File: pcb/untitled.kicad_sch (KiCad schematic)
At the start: 6 parts, among them Q1 NMOS, Q2 PMOS

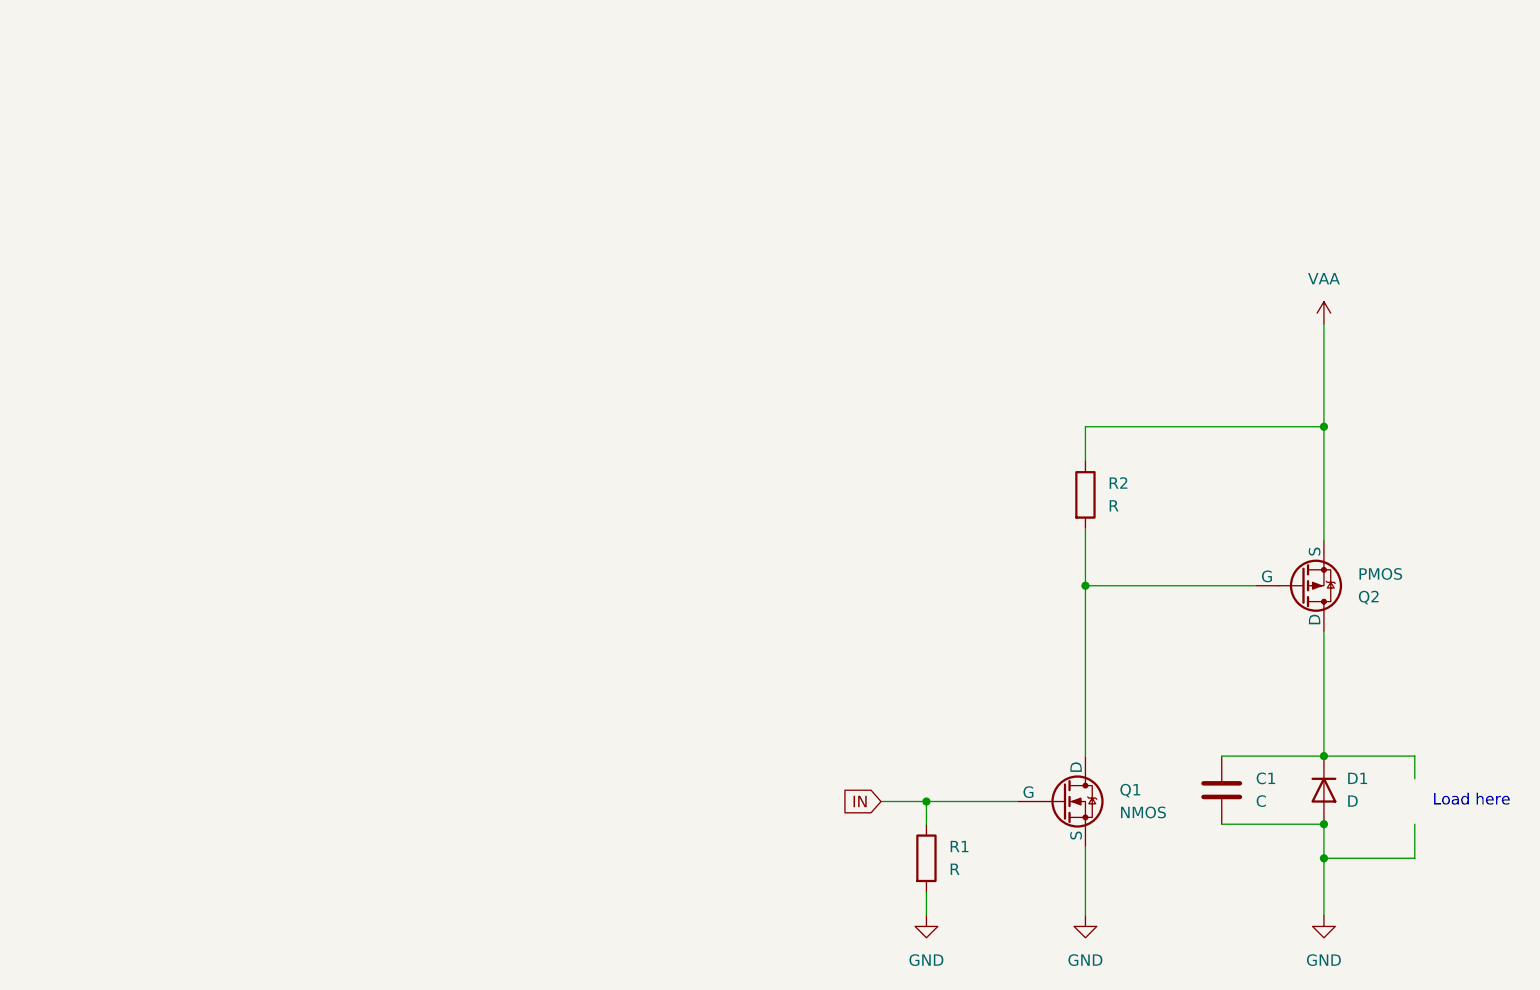
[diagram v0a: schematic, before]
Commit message: Upload of rcs controller board 1st draft
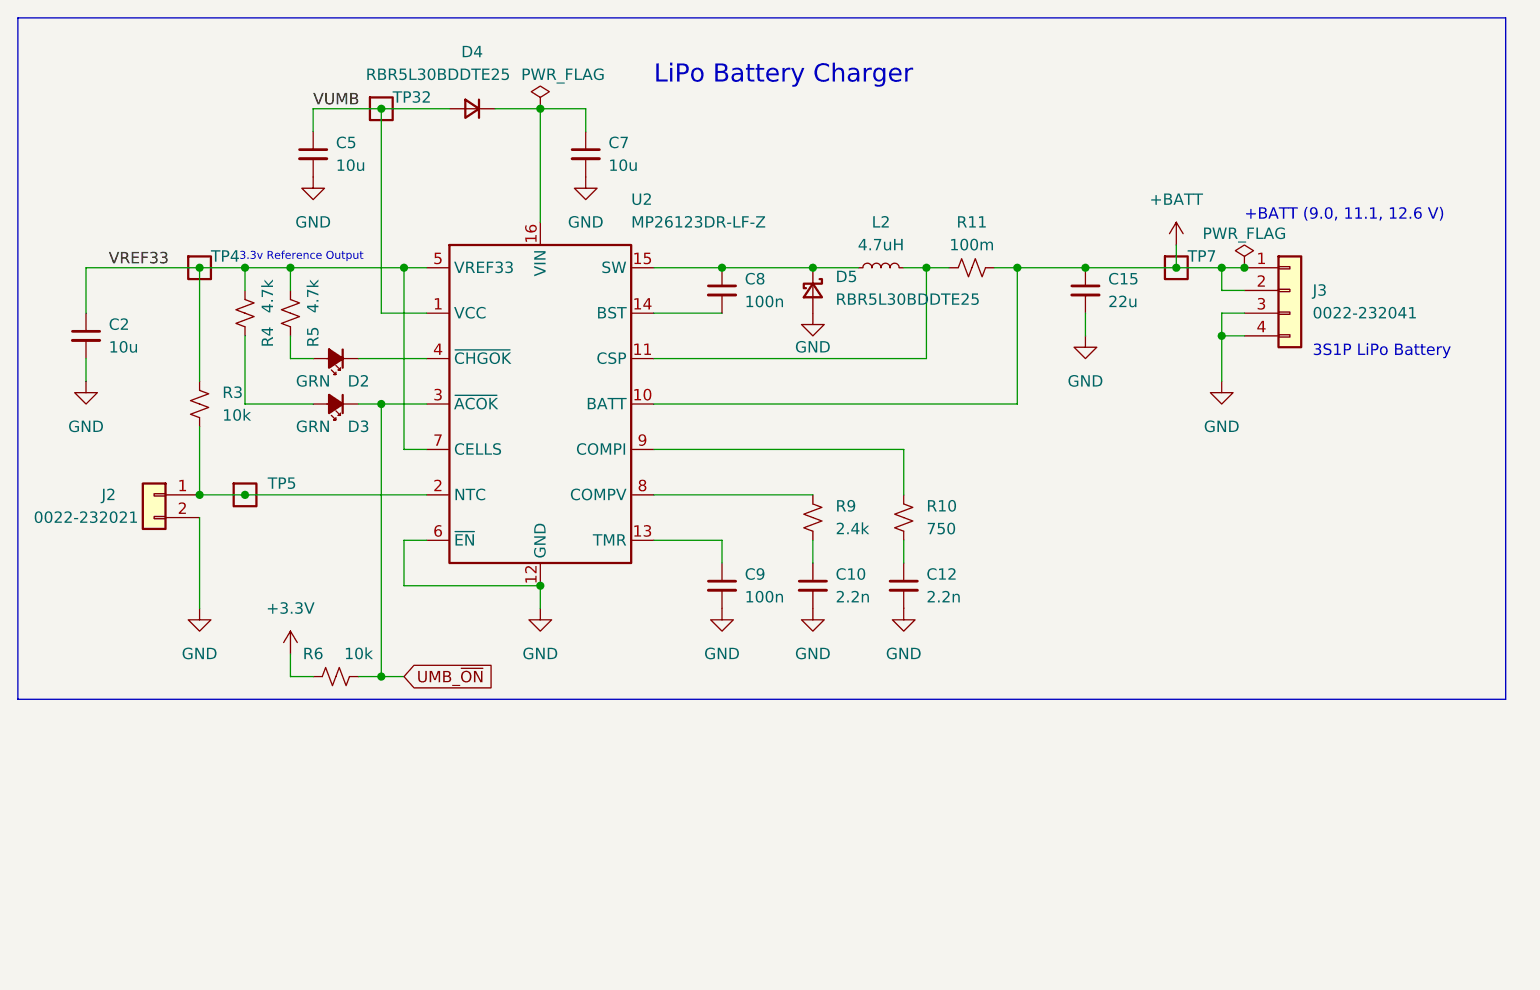
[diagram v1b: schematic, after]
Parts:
- removed C1: C, symbol Device:C
- removed D1: D, symbol Device:D
- removed Q1: NMOS, symbol Simulation_SPICE:NMOS
- removed Q2: PMOS, symbol Simulation_SPICE:PMOS
- removed R1, R2: R, symbol Device:R
- added C10, C12: 2.2n, Capacitor_SMD:C_0603_1608Metric, symbol Device:C_Small
- added C15: 22u, Capacitor_SMD:C_0805_2012Metric, symbol Device:C_Small
- added C2, C5, C7: 10u, Capacitor_SMD:C_0805_2012Metric, symbol Device:C_Small
- added C8, C9: 100n, Capacitor_SMD:C_0603_1608Metric, symbol Device:C_Small
- added D2, D3: GRN, LED_SMD:LED_0603_1608Metric, symbol Device:LED_Small_Filled
- added D4: RBR5L30BDDTE25, Diode_SMD:D_SMA, symbol Device:D_Small
- added D5: RBR5L30BDDTE25, Diode_SMD:D_SMA, symbol Device:D_Schottky_Small
- added J2: 0022-232021, Connector_Molex:Molex_KK-254_AE-6410-02A_1x02_P2.54mm_Vertical, symbol Connector_Generic:Conn_01x02
- added J3: 0022-232041, Connector_Molex:Molex_KK-254_AE-6410-04A_1x04_P2.54mm_Vertical, symbol Connector_Generic:Conn_01x04
- added L2: 4.7uH, Inductor_SMD:L_Vishay_IHLP-2020, symbol Device:L_Small
- added R10: 750, Resistor_SMD:R_0603_1608Metric, symbol Device:R_Small_US
- added R11: 100m, Resistor_SMD:R_1206_3216Metric, symbol Device:R_Small_US
- added R3, R6: 10k, Resistor_SMD:R_0603_1608Metric, symbol Device:R_Small_US
- added R4, R5: 4.7k, Resistor_SMD:R_0603_1608Metric, symbol Device:R_Small_US
- added R9: 2.4k, Resistor_SMD:R_0603_1608Metric, symbol Device:R_Small_US
- added TP32, TP4, TP5, TP7: Test-Point, psas-footprints:TP-through-hole-1X01, symbol psas-testpoint:Test-Point
- added U2: MP26123DR-LF-Z, Package_DFN_QFN:QFN-16-1EP_4x4mm_P0.65mm_EP2.5x2.5mm, symbol U-MonolithicPower-MP26123DR-LF-Z-battery-charger-li-ion:MP26123DR-LF-Z
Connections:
- net GND: now also C10.2, C12.2, C15.2, C2.2, C5.2, C7.2, C9.2, D5.2 (A), J2.2 (Pin_2), J3.3 (Pin_3), J3.4 (Pin_4), U2.12 (GND), U2.17 (GND), U2.6 (~{EN})
- new net: C12.1, R10.2
- new net: D3.2 (A), R4.2
- new net: C8.1, D5.1 (K), L2.1, U2.15 (SW)
- new net: L2.2, R11.1, U2.11 (CSP)
- new net: R9.1, U2.8 (COMPV)
- new net: C10.1, R9.2
- new net: D2.1 (K), U2.4 (~{CHGOK})
- new net: D2.2 (A), R5.2
- new net: J2.1 (Pin_1), R3.2, TP5.1, U2.2 (NTC)
- new net: C7.1, D4.1 (K), U2.16 (VIN)
- new net: C8.2, U2.14 (BST)
- new net: C9.1, U2.13 (TMR)
- new net: R10.1, U2.9 (COMPI)
- new net +3.3V: R6.1
- new net +BATT: C15.1, J3.1 (Pin_1), J3.2 (Pin_2), R11.2, TP7.1, U2.10 (BATT)
- new net UMB_~{ON}: D3.1 (K), R6.2, U2.3 (~{ACOK})
- new net VREF33: C2.1, R3.1, R4.1, R5.1, TP4.1, U2.5 (VREF33), U2.7 (CELLS)
- new net VUMB: C5.1, D4.2 (A), TP32.1, U2.1 (VCC)
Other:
- note added: "+BATT (9.0, 11.1, 12.6 V)"
- note added: "3.3v Reference Output"
- note added: "3S1P LiPo Battery"
- note added: "LiPo Battery Charger"
- note removed: "Load here"

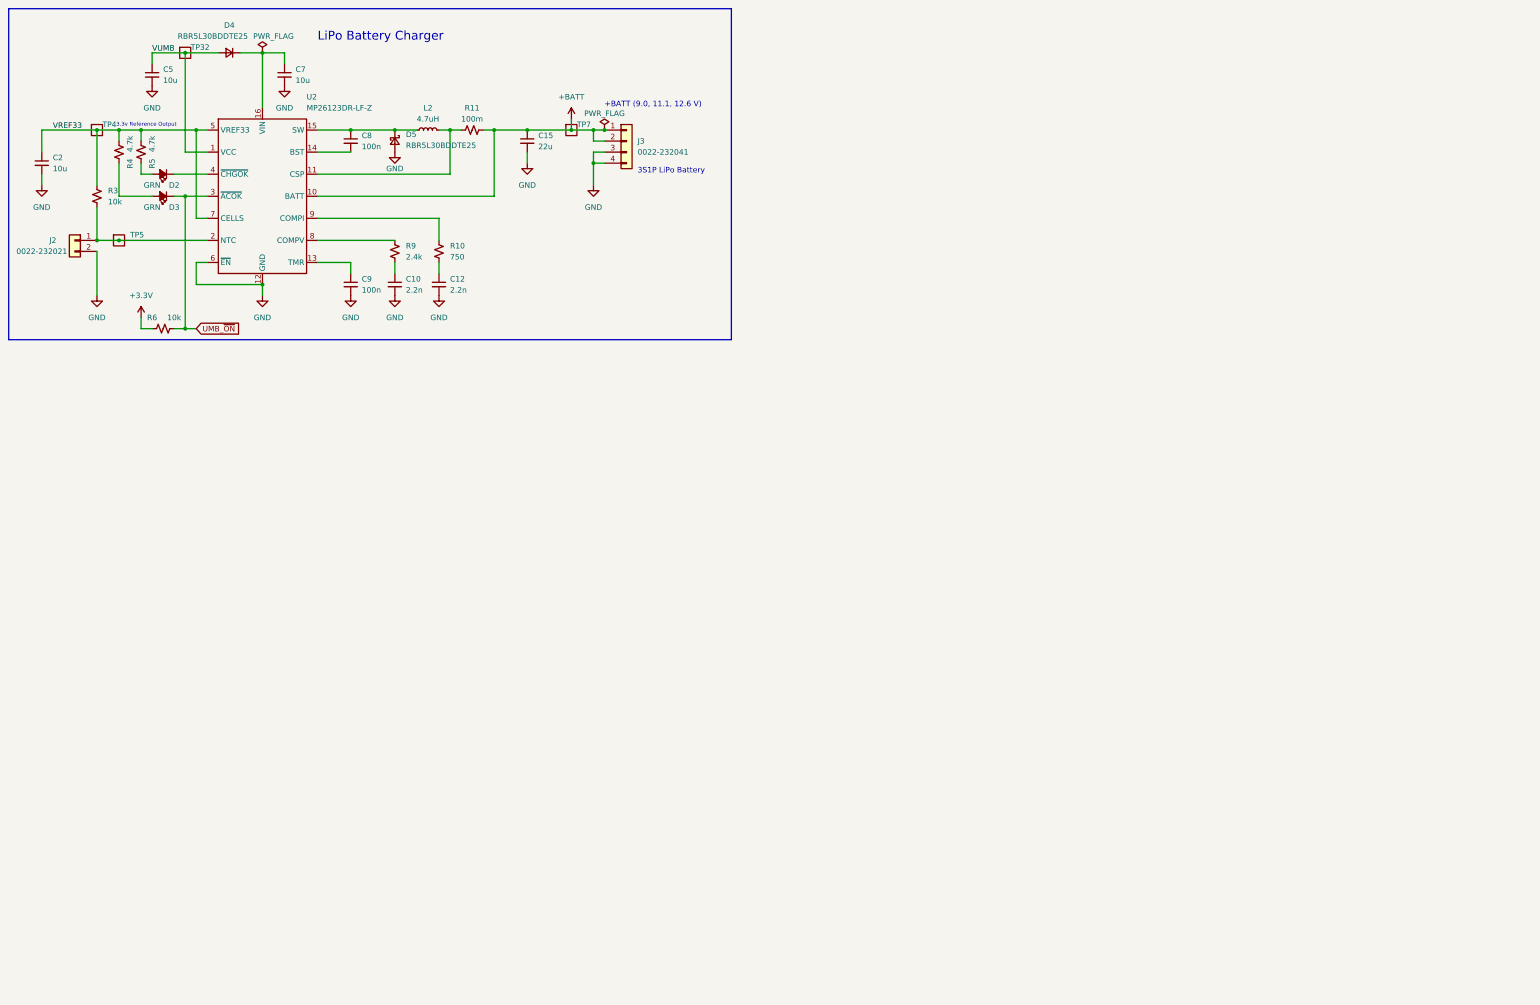
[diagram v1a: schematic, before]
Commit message: Updated with footprint and more fleshed out circuit
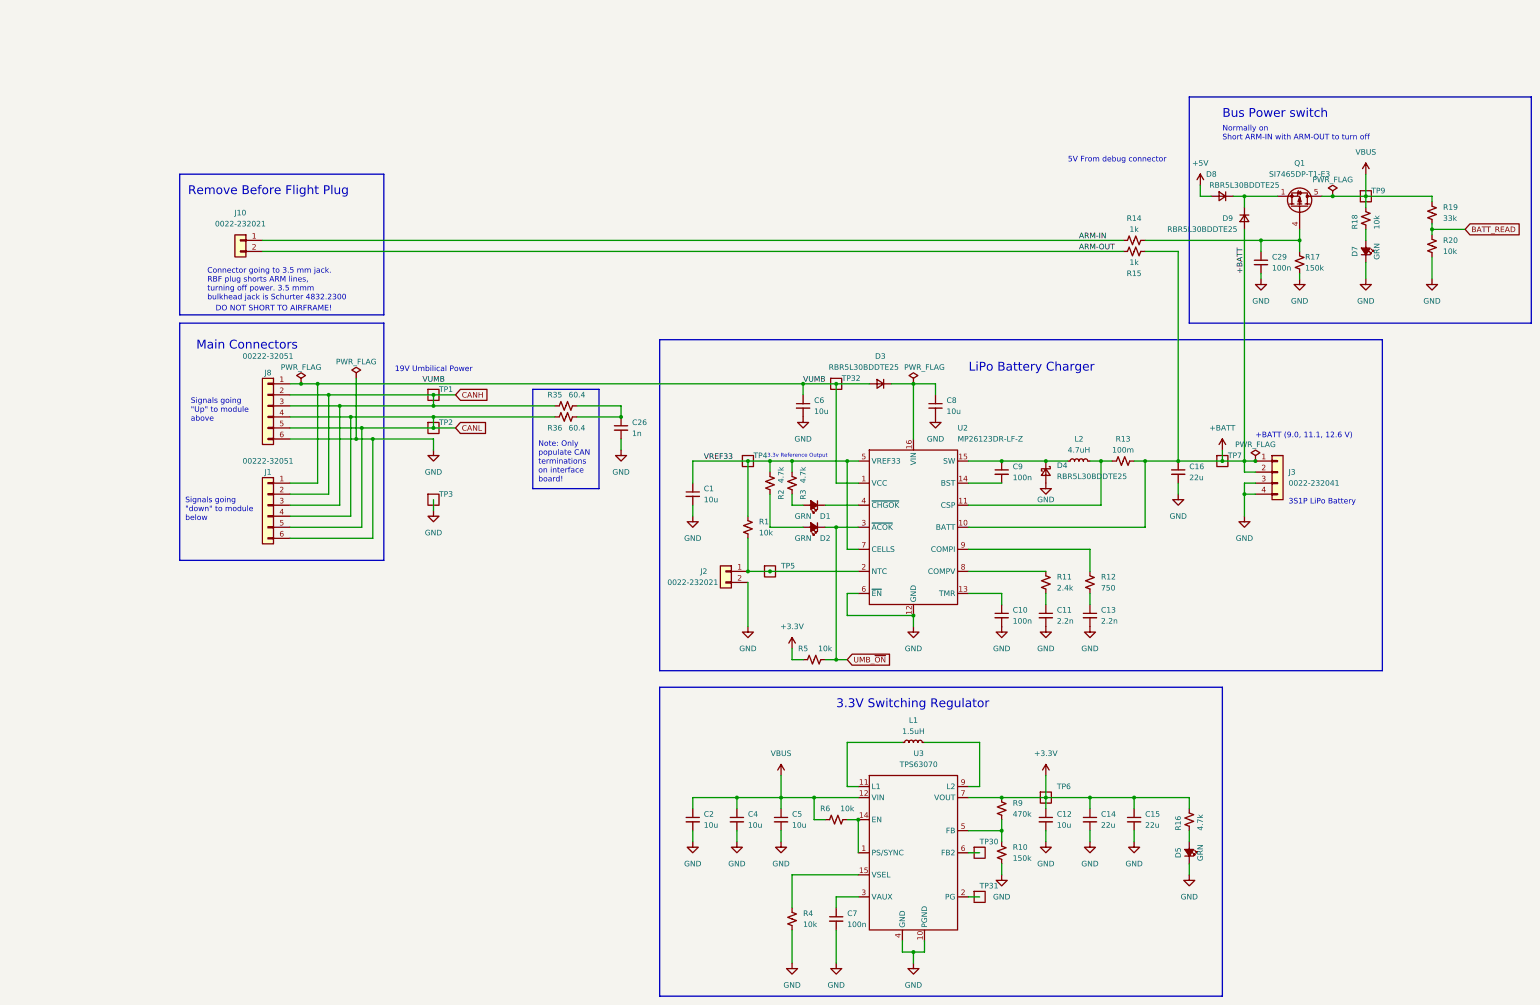
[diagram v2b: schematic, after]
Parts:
- removed D2: GRN, LED_SMD:LED_0603_1608Metric, symbol Device:LED_Small_Filled
- removed R3: 10k, Resistor_SMD:R_0603_1608Metric, symbol Device:R_Small_US
- added C1, C4: 10u, Capacitor_SMD:C_0805_2012Metric, symbol Device:C_Small
- added C12, C5: 10u, Capacitor_SMD:C_0603_1608Metric, symbol Device:C_Small
- added C14, C15: 22u, Capacitor_SMD:C_0805_2012Metric, symbol Device:C_Small
- added C26: 1n, Capacitor_SMD:C_0603_1608Metric, symbol Device:C_Small
- added C29, C7: 100n, Capacitor_SMD:C_0603_1608Metric, symbol Device:C_Small
- added D1, D5, D7: GRN, LED_SMD:LED_0603_1608Metric, symbol Device:LED_Small_Filled
- added D8, D9: RBR5L30BDDTE25, Diode_SMD:D_SMA, symbol Device:D_Small
- added J1, J8: 00222-32051, Connector_Molex:Molex_KK-254_AE-6410-06A_1x06_P2.54mm_Vertical, symbol Connector_Generic:Conn_01x06
- added J10: 0022-232021, Connector_Molex:Molex_KK-254_AE-6410-02A_1x02_P2.54mm_Vertical, symbol Connector_Generic:Conn_01x02
- added L1: 1.5uH, Inductor_SMD:L_Vishay_IHLP-2020, symbol Device:L_Small
- added Q1: SI7465DP-T1-E3, psas-footprints:PowerPAK_SO-8_Single, symbol Transistor_FET:Si7141DP
- added R1, R18, R20, R6: 10k, Resistor_SMD:R_0603_1608Metric, symbol Device:R_Small_US
- added R10, R17: 150k, Resistor_SMD:R_0603_1608Metric, symbol Device:R_Small_US
- added R14, R15: 1k, Resistor_SMD:R_0603_1608Metric, symbol Device:R_Small_US
- added R16, R2: 4.7k, Resistor_SMD:R_0603_1608Metric, symbol Device:R_Small_US
- added R19: 33k, Resistor_SMD:R_0603_1608Metric, symbol Device:R_Small_US
- added R35, R36: 60.4, Resistor_SMD:R_1206_3216Metric, symbol Device:R_Small_US
- added R9: 470k, Resistor_SMD:R_0603_1608Metric, symbol Device:R_Small_US
- added TP1, TP2, TP3, TP30, TP31, TP6, TP9: Test-Point, psas-footprints:TP-through-hole-1X01, symbol psas-testpoint:Test-Point
- added U3: TPS63070, psas-footprints:U-TI-TPS63070, symbol U-TI-TPS63070x-buck-boost-regulator:TPS63070
- R4: value 4.7k -> 10k; DPN 311-4.70KHRCT-ND -> 311-10.0KHRCT-ND; MPN RC0603FR-074K7L -> RC0603FR-0710KL
- renumbered C9 to C10, C10 to C11, C12 to C13, C15 to C16, C5 to C6, C7 to C8, C8 to C9, D3 to D2, D4 to D3, D5 to D4, R9 to R11, R10 to R12, R11 to R13, R5 to R3, R6 to R5
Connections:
- net +3.3V: now also C12.1, C14.1, C15.1, R16.1, R9.1, TP6.1, U3.7 (VOUT), U3.8 (VOUT), U3.TIE2 (VOUT)
- net +BATT: now also D9.2 (A), R15.1
- net GND: now also R4.2, C1.2, C12.2, C14.2, C15.2, C26.2, C29.2, C4.2, C5.2, C7.2, D5.1 (K), D7.1 (K), J1.6 (Pin_6), J8.6 (Pin_6), R10.2, R17.2, R20.2, TP3.1, U3.10 (PGND), U3.4 (GND)
- net VREF33: now also C1.1, R1.1, R2.1; no longer C2.1, R4.1
- net VUMB: now also J1.1 (Pin_1), J8.1 (Pin_1)
- net at D2.2 (A): now also R2.2; no longer R4.2
- net at U2.4 (~{CHGOK}): now also D1.1 (K)
- net at R3.2: now also D1.2 (A)
- net at J2.1 (Pin_1), TP5.1, U2.2 (NTC): now also R1.2
- new net: C29.1, Q1.4 (G), R14.2, R17.1
- new net: D5.2 (A), R16.2
- new net: D8.1 (K), D9.1 (K), Q1.1 (S), Q1.2 (S), Q1.3 (S)
- new net: R10.1, R9.2, U3.5 (FB)
- new net: R4.1, U3.15 (VSEL)
- new net: D7.2 (A), R18.2
- new net: C26.1, R35.2, R36.1
- new net: R6.2, U3.1 (PS/SYNC), U3.14 (EN)
- new net: L1.1, U3.11 (L1)
- new net: L1.2, U3.9 (L2)
- new net: TP31.1, U3.2 (PG)
- new net: C7.1, U3.3 (VAUX)
- new net: TP30.1, U3.6 (FB2)
- new net +5V: D8.2 (A)
- new net ARM-IN: J10.1 (Pin_1), R14.1
- new net ARM-OUT: J10.2 (Pin_2), R15.2
- new net BATT_READ: R19.2, R20.1
- new net CANH: J1.2 (Pin_2), J1.3 (Pin_3), J8.2 (Pin_2), J8.3 (Pin_3), R35.1, TP1.1
- new net CANL: J1.4 (Pin_4), J1.5 (Pin_5), J8.4 (Pin_4), J8.5 (Pin_5), R36.2, TP2.1
- new net VBUS: C2.1, C4.1, C5.1, Q1.5 (D), R18.1, R19.1, R6.1, TP9.1, U3.12 (VIN), U3.13 (VIN), U3.TIE1 (VIN)
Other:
- note added: "19V Umbilical Power"
- note added: "3.3V Switching Regulator"
- note added: "5V From debug connector"
- note added: "Bus Power switch"
- note added: "Connector going to 3.5 mm jack. RBF plug shorts ARM lines, turning off power. 3.5 mmm bulkhead jack is Schurter 4832.2300"
- note added: "DO NOT SHORT TO AIRFRAME!"
- note added: "Main Connectors"
- note added: "Normally on Short ARM-IN with ARM-OUT to turn off"
- note added: "Note: Only populate CAN terminations on interface board!"
- note added: "Remove Before Flight Plug"
- note added: "Signals going "Up" to module above"
- note added: "Signals going "down" to module below"
- title: (none) -> RCS Controller Board
- moved on the sheet: C10, C11, C13, C16, C6, C8, C9, D2, D3, D4, J2, J3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
